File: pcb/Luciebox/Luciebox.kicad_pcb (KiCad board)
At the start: 2 copper layers, 100 x 100 mm, 93 parts, among them J1 Screw_Terminal_01x07, J2 Screw_Terminal_01x07, J3 Screw_Terminal_01x07, J4 Screw_Terminal_01x07, J5 Screw_Terminal_01x07, J7 USB_B_Mini, P1 CONN_01X01, P2 CONN_01X01, P3 CONN_01X01, P4 CONN_01X01, P5 Digital, P6 Power, P7 Digital, P8 Analog, Q1 BC558, Q2 N-Channel_Mosfet, SW10 Switch_tilt, SW11 Switch_tilt, SW12 Switch_tilt, SW9 Switch_tilt, T1 terminal_13x1, T11 terminal_3x1, T2 terminal_8x1, T3 terminal_8x1, T4 terminal_8x1, T5 terminal_8x1, T6 terminal_8x1, T7 terminal_8x1, T8 terminal_3x1, U1 CA56-12SRWA, U2 ULN2003A, U3 ATmega328-PU, U4 8X8PADS, Y1 16MHz

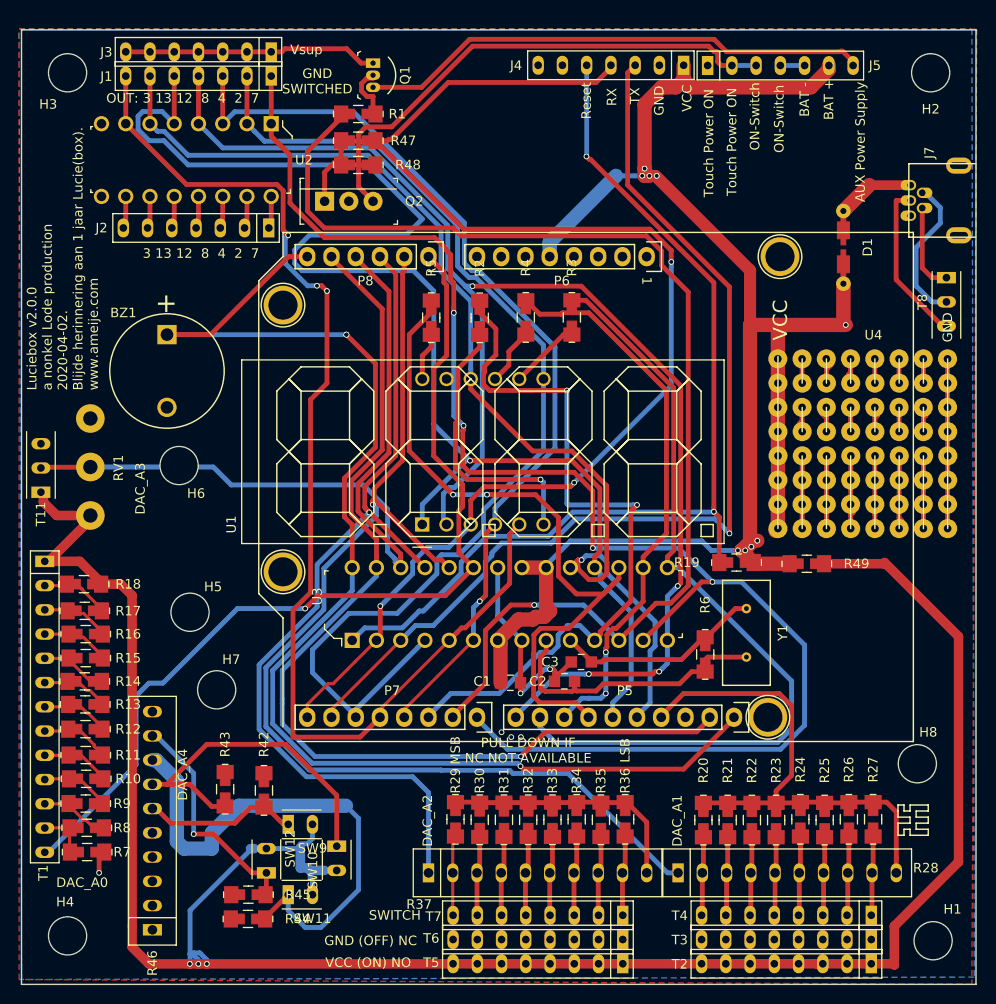
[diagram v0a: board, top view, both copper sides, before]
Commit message: add holes for R-2R ladder, fix bug with tilt switch sheet. Set output led's. All good here.
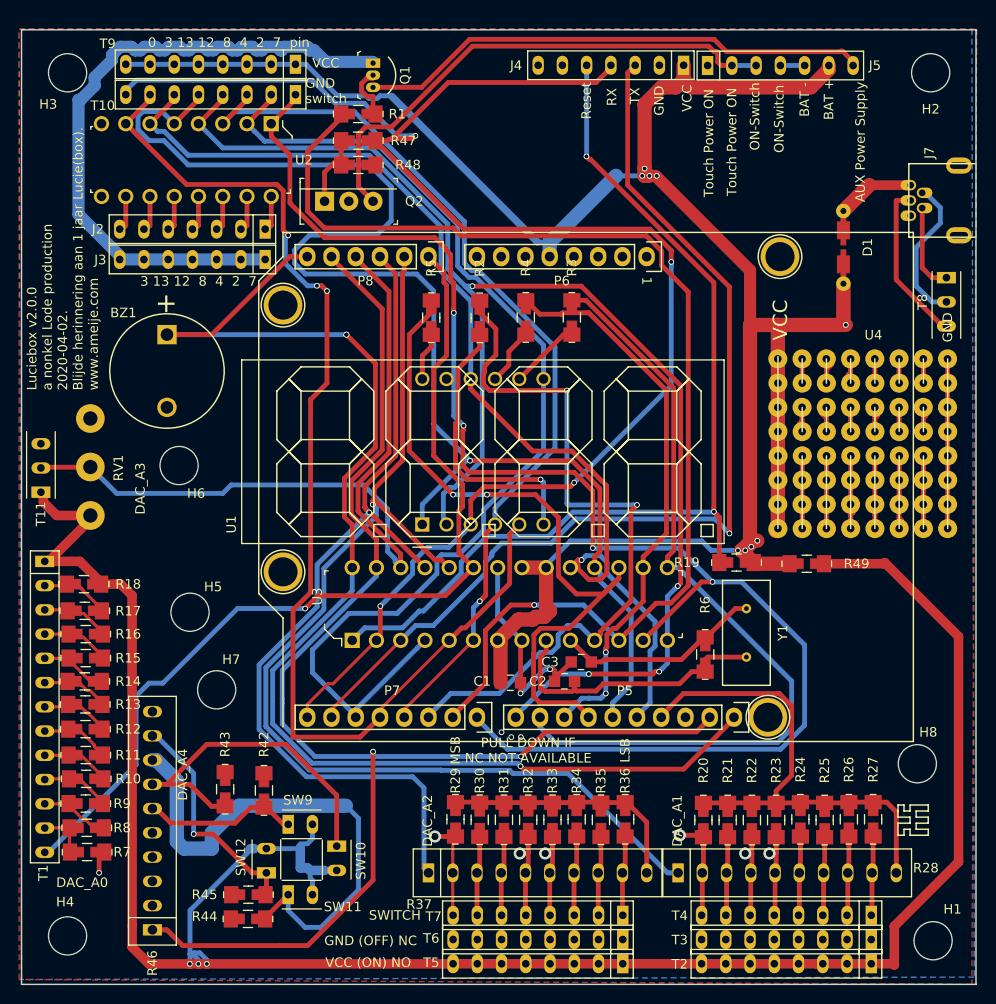
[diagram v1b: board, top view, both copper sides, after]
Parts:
- removed J1: Screw_Terminal_01x07, Luciebox:Terminal_7x1_100mil
- added T10: terminal_8x1, Luciebox:Terminal_8x1_100mil, F.Cu at (20.1, 7.00)
- added T9: terminal_8x1, Luciebox:Terminal_8x1_100mil, F.Cu at (20.1, 3.82)
- moved J3 21.8 mm to (18.2, 24.3)
- moved J2 0.40 mm to (18.2, 21.1)
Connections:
- R46 pad 1: Net-(R46-Pad1) -> /A4(SDA)
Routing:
- net VCC: track 178.1 -> 230.5 mm
- net Net-(J3-Pad1): track 27.5 -> 71.0 mm
- net /A4(SDA): track 105.7 -> 146.4 mm, vias 1 -> 2
- net /0(Rx): track 136.1 -> 172.3 mm, vias 3 -> 4
- net /12(MISO): track 146.2 -> 140.9 mm
- net Net-(R20-Pad1): track 8.26 -> 10.8 mm, vias 0 -> 1
- net Net-(R29-Pad1): track 8.24 -> 10.4 mm, vias 0 -> 1
- net Net-(R32-Pad1): track 8.34 -> 9.28 mm, vias 0 -> 1
- net /7: track 159.0 -> 158.1 mm
- net /3(PWM): track 122.6 -> 121.7 mm
- net /2: track 114.2 -> 113.3 mm
- net /13(SCK): track 114.2 -> 113.4 mm
- net /8: track 145.3 -> 144.5 mm
- net /4: track 98.3 -> 97.5 mm
- net Net-(R33-Pad1): track 8.34 -> 9.15 mm, vias 0 -> 1
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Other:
- board text added: "0 3 13 12 8 4 2 7 pin"
- board text added: "GND switch"
- board text removed: "GND SWITCHED"
- board text removed: "OUT: 3 13 12 8 4 2 7"
- board text removed: "Vsup"

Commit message: modify pcb v2.0.  nearly finished. Choose box.
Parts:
- added T12: terminal_8x1, Luciebox:Terminal_8x1_100mil, F.Cu at (80.0, 78.2)
- moved R19 1.90 mm to (75.2, 57.9)
- moved R49 1.78 mm to (82.5, 57.9)
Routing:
- net /13(SCK): track 113.4 -> 164.2 mm
- net /3(PWM): track 121.7 -> 172.1 mm, vias 3 -> 0
- net /4: track 97.5 -> 137.0 mm
- net /0(Rx): track 172.3 -> 211.7 mm
- net /2: track 113.3 -> 152.6 mm, vias 0 -> 1
- net /8: track 144.5 -> 180.4 mm, vias 4 -> 5
- net /12(MISO): track 140.9 -> 171.2 mm, vias 1 -> 3
- net Net-(R44-Pad2): track 55.3 -> 27.7 mm
- net VCC_minimalCurrent: track 232.9 -> 210.5 mm, vias 3 -> 1
- net GND: track 124.1 -> 108.4 mm, vias 6 -> 5
- net VCC: track 230.5 -> 245.8 mm, vias 9 -> 8
- net /1(Tx): track 106.1 -> 92.5 mm
- net /A2: track 94.2 -> 86.6 mm
- net /5(PWM): track 77.1 -> 69.9 mm, vias 2 -> 0
- net /A0: track 97.5 -> 103.1 mm
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
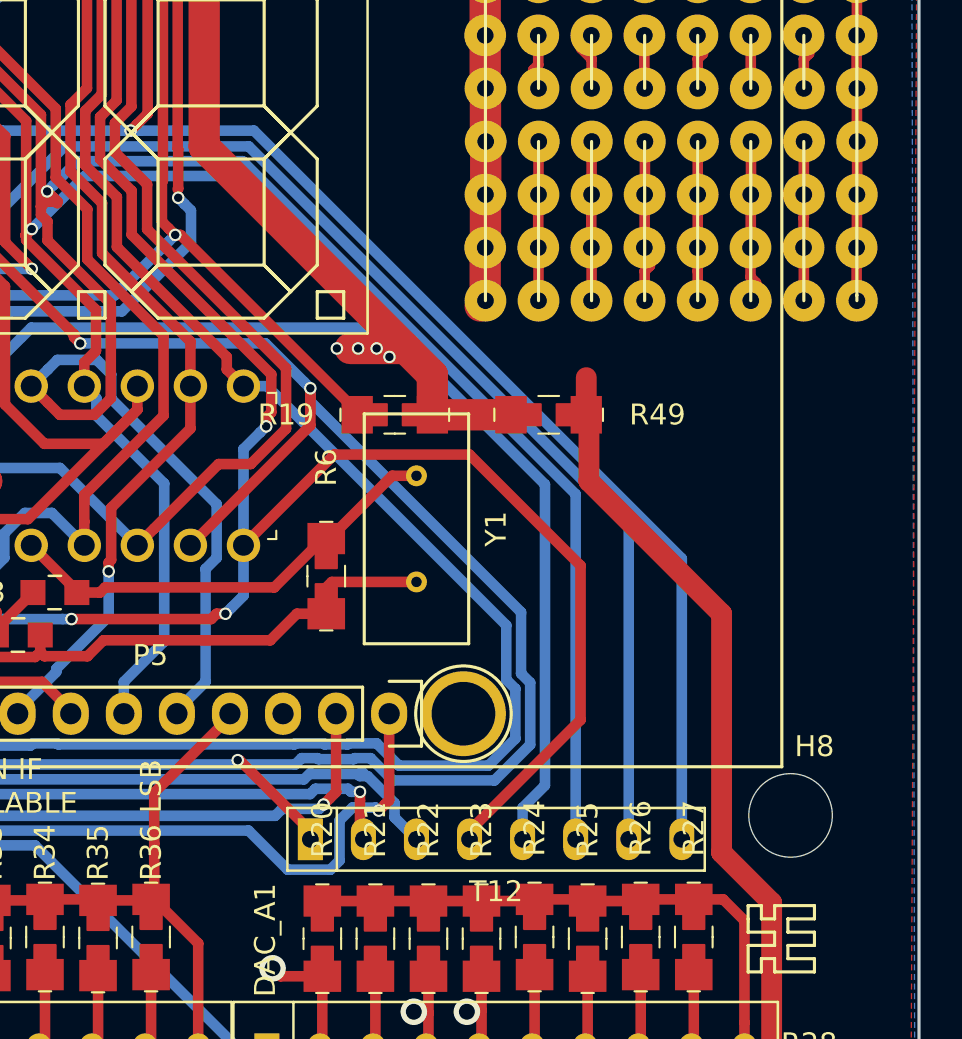
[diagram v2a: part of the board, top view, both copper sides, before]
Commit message: pcb change extra header so holes line up for lights to buttons.
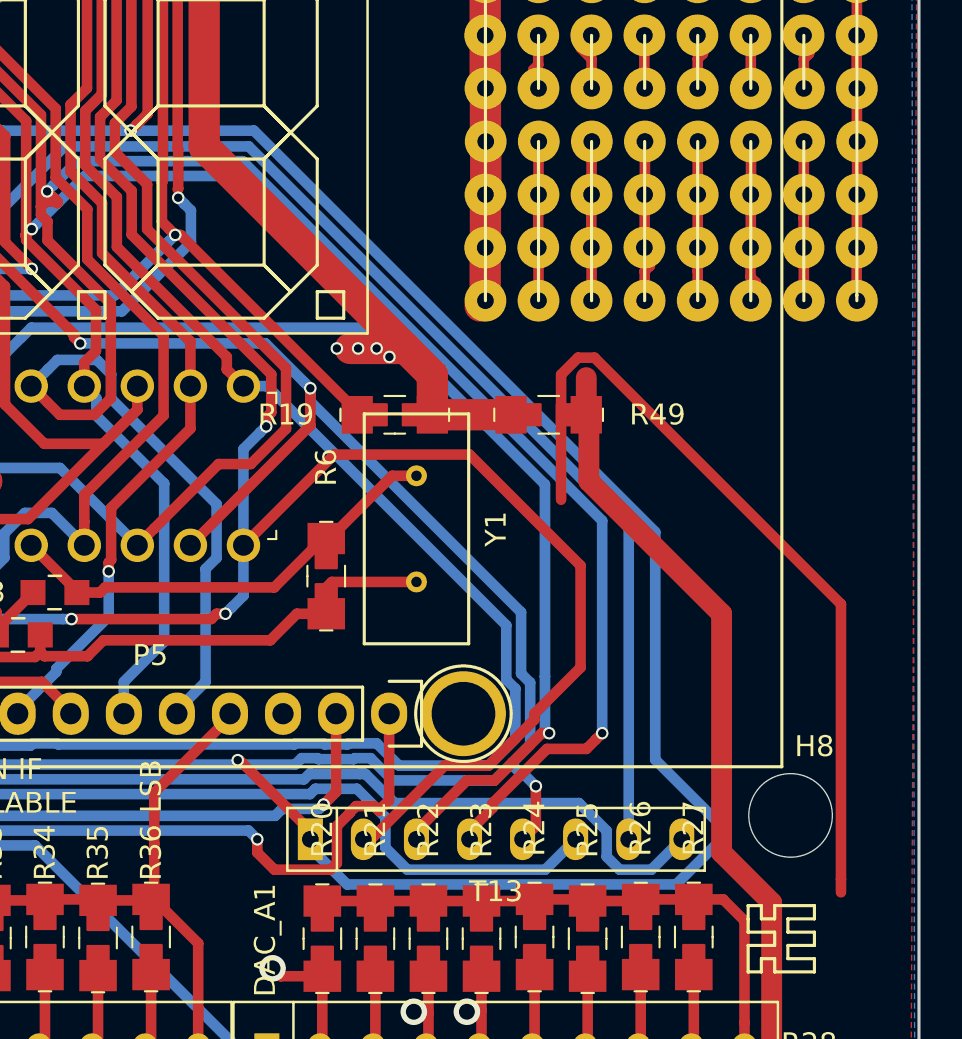
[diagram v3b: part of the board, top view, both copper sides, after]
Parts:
- removed T12: terminal_8x1, Luciebox:Terminal_8x1_100mil
- added T13: terminal_8x1, Luciebox:Terminal_8x1_100mil, F.Cu at (80.0, 78.2)
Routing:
- net (no net): track 0.00 -> 38.4 mm
- net /0(Rx): track 211.7 -> 234.2 mm
- net /4: track 137.0 -> 150.5 mm
- net /2: track 152.6 -> 163.6 mm, vias 1 -> 0
- net /7: track 162.1 -> 166.6 mm, vias 3 -> 4
- net /13(SCK): track 164.2 -> 168.5 mm, vias 1 -> 2
- net /12(MISO): track 171.2 -> 175.0 mm, vias 3 -> 4
- net /8: track 180.4 -> 184.2 mm

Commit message: pcb finish v2.0
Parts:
- added ?: , artwork:virus_corona, B.Cu at (50.8, 49.7)
- added G***: LOGO, artwork:titles_and_text, F.Cu at (47.0, 46.5)
- added G***: LOGO, artwork:virus_corona3, F.Cu at (50.2, 50.3)
- added G***: LOGO, artwork:virus_corona2, F.Cu at (50.2, 49.7)
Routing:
- net (no net): track 38.4 -> 0.00 mm
- net /7: track 166.6 -> 161.4 mm
- net VCC_minimalCurrent: track 210.5 -> 208.7 mm
